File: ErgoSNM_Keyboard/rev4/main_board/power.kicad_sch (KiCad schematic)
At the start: 28 parts, among them SW3 SW_DPDT_x2, SW4 SW_DPDT_x2, U1 BQ24075RGT, U2 TPS63020

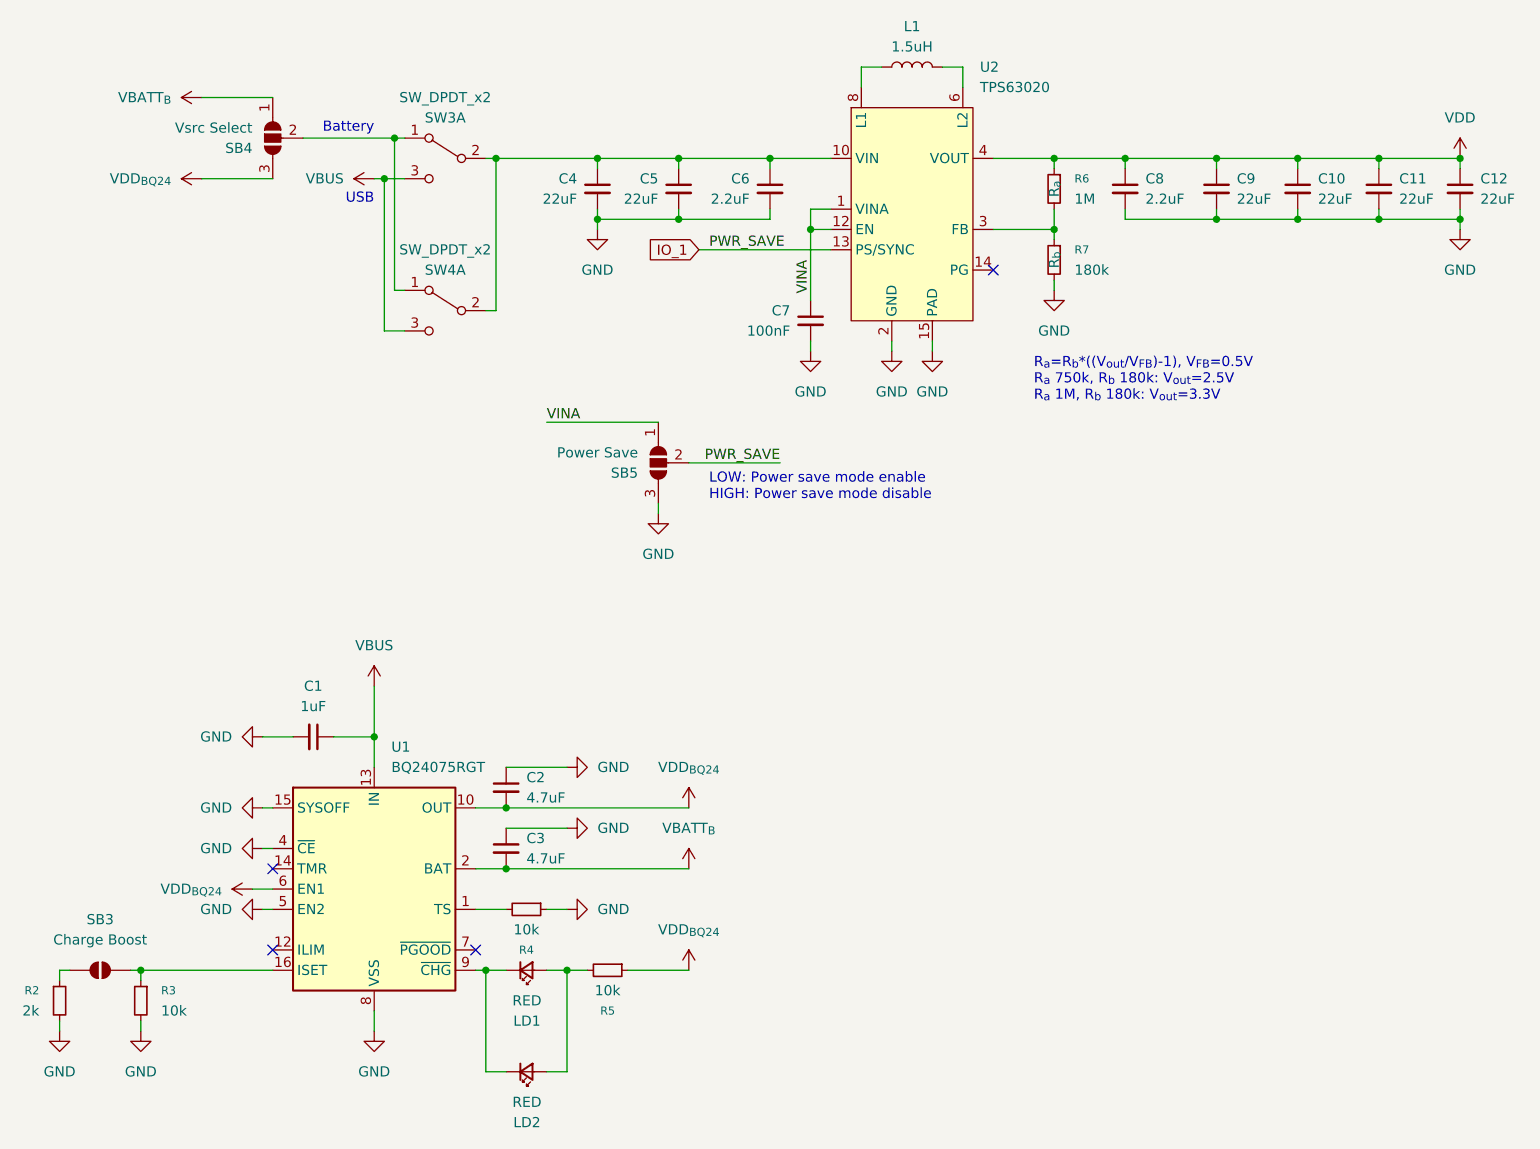
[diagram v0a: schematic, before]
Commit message: feat: add v4 mdbt50q board
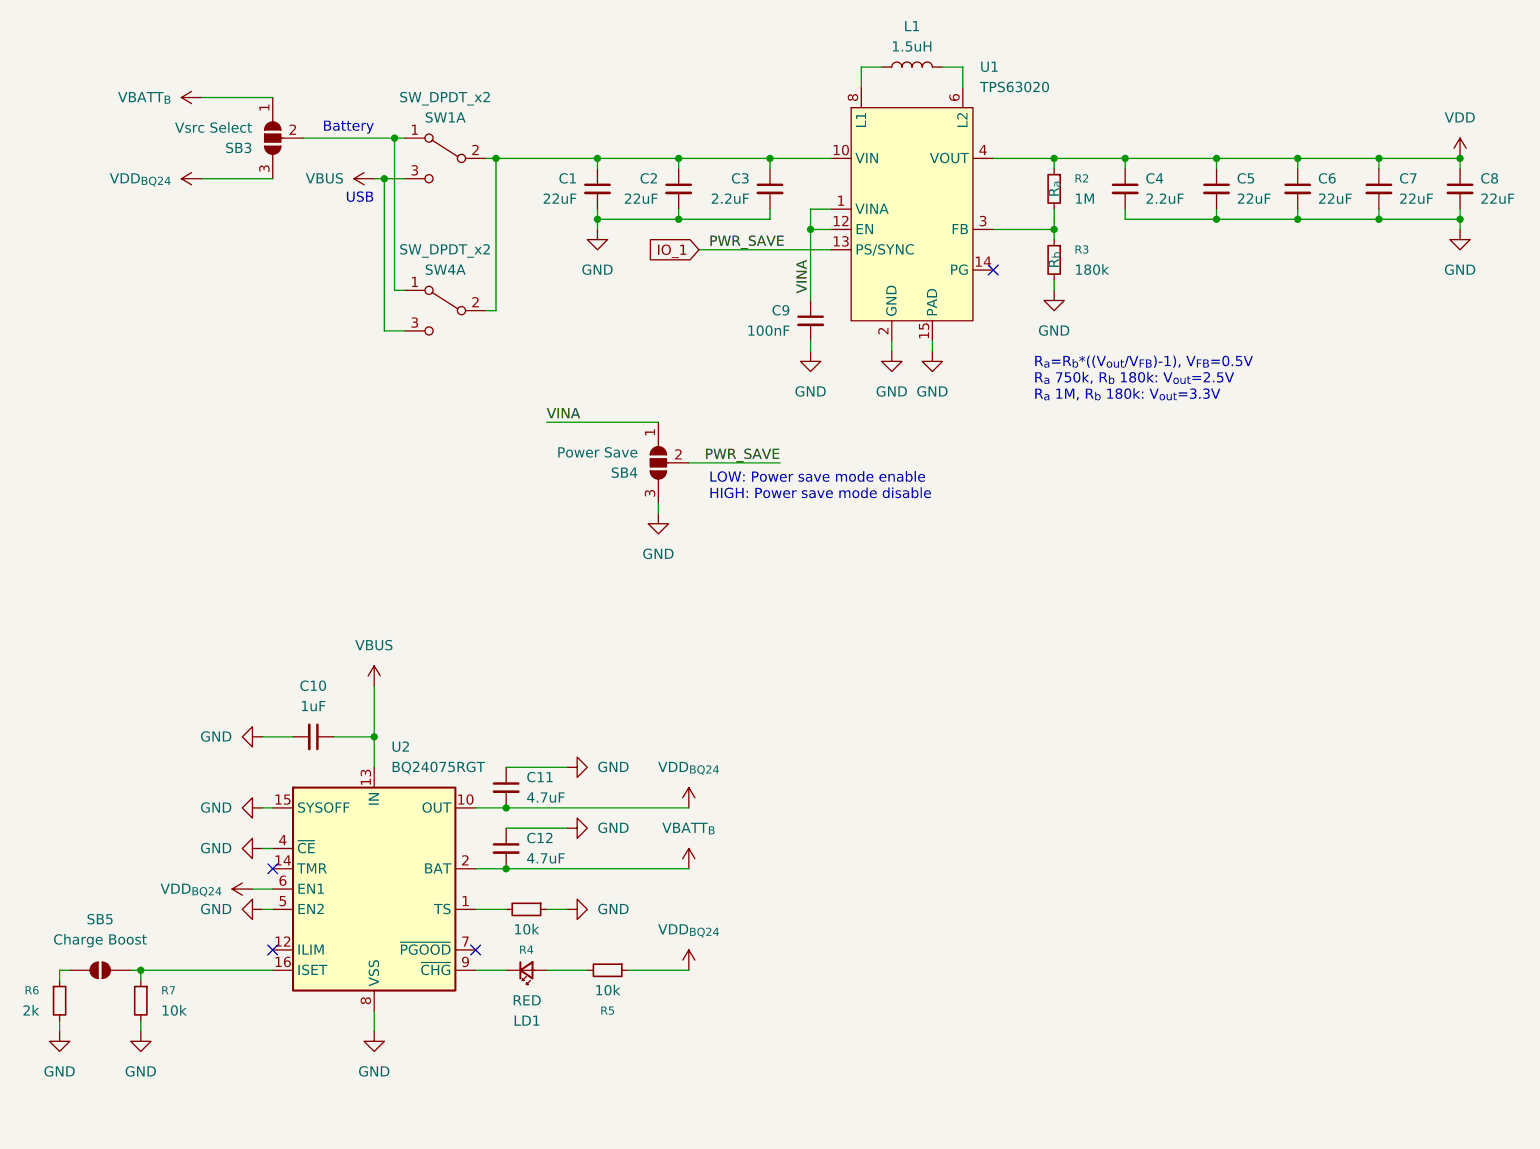
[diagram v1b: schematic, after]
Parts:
- removed LD2: RED, LED_SMD:LED_0603_1608Metric, symbol Device:LED_Small
- SB3: renamed from SB4; footprint Jumper:SolderJumper-2_P1.3mm_Open_TrianglePad1.0x1.5mm -> Jumper:SolderJumper-3_P2.0mm_Open_TrianglePad1.0x1.5mm_NumberLabels
- SB4: renamed from SB5; footprint Jumper:SolderJumper-2_P1.3mm_Open_TrianglePad1.0x1.5mm -> Jumper:SolderJumper-3_P2.0mm_Open_TrianglePad1.0x1.5mm_NumberLabels
- renumbered C4 to C1, C1 to C10, C2 to C11, C3 to C12, C5 to C2, C6 to C3, C8 to C4, C9 to C5, C10 to C6, C11 to C7, C12 to C8, C7 to C9, R6 to R2, R7 to R3, R2 to R6, R3 to R7, SB3 to SB5, SW3 to SW1, U2 to U1, U1 to U2
